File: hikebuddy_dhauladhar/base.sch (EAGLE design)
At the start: 119 parts, among them J1 MF-CON-MICROUSB-RIGHT, J2 GPS Port, J5 SOLDER_PAD_2, J9 47352-1001, U1 LTC3586EUFE-1#PBF, U2 MAX17260SETD+, U3 MF-DSC-SOT233-MMBT3904, U4 MF-DSC-SOT233-MMBT3904, U5 DRV2605LTDGSRQ1, U7 LSM303CTR, U9 LTC6991CDCB#TRMPBF

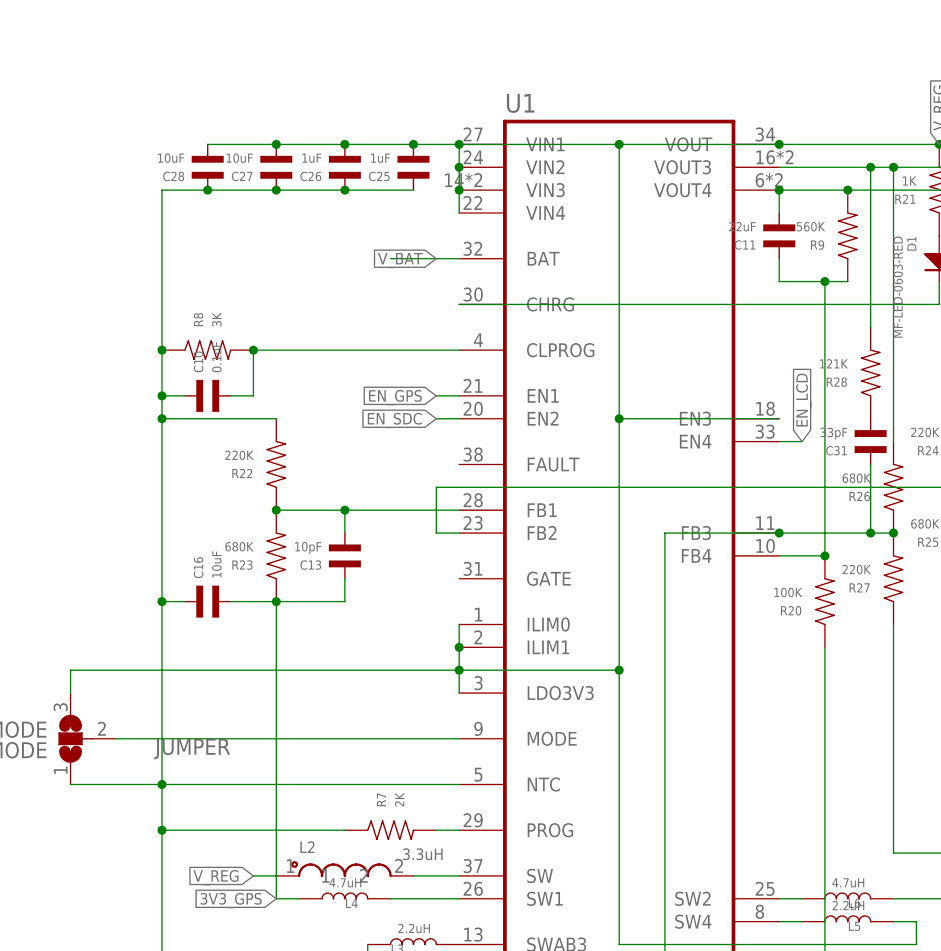
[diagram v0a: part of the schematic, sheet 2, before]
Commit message: pulled up fault and EN to V_REG to fix startup bug
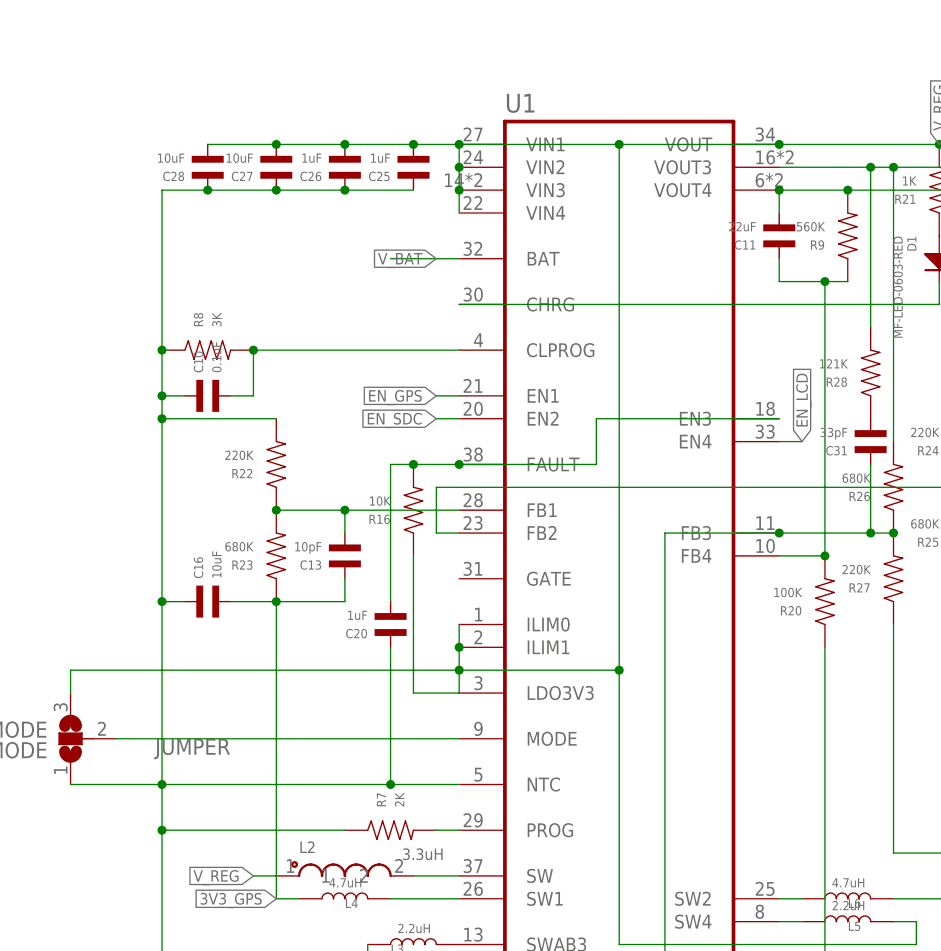
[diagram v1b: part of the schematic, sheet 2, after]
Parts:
- added C20: 1uF, MF_Passives:CAPACITOR_NP_0603
- added R16: 10K, MF_Passives:RESISTOR_0603
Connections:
- new net N$24: C20.P$2, R16.P$2, U1.EN3, U1.FAULT
- net GND: now also C20.P$1
- net V_REG: now also R16.P$1; no longer U1.EN3
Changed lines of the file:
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@@
 <part name="J9" library="47352-1001" deviceset="47352-1001" device="" package3d_urn="urn:adsk.eagle:package:16346114/2"/>
 <part name="GND19" library="supply1" library_urn="urn:adsk.eagle:library:371" deviceset="GND" device=""/>
+<part name="R16" library="MF_Passives" deviceset="RESISTOR" device="_0603" package3d_urn="urn:adsk.eagle:package:16347927/2" value="10K"/>
+<part name="C20" library="MF_Passives" deviceset="CAPACITOR_NP" device="_0603" package3d_urn="urn:adsk.eagle:package:16347923/3" value="1uF"/>
 </parts>
 <sheets>
@@
 <attribute name="VALUE" x="152.4" y="9.906" size="1.778" layer="96" align="top-center"/>
 </instance>
+<instance part="R16" gate="G$1" x="53.34" y="78.74" smashed="yes" rot="R180">
+<attribute name="NAME" x="50.8" y="77.216" size="1.016" layer="95" font="vector" rot="R180" align="top-left"/>
+<attribute name="VALUE" x="50.8" y="80.264" size="1.016" layer="96" font="vector" rot="R180"/>
+</instance>
+<instance part="C20" gate="G$1" x="50.8" y="66.04" smashed="yes" rot="R180">
+<attribute name="NAME" x="48.26" y="64.516" size="1.016" layer="95" font="vector" rot="R180" align="top-left"/>
+<attribute name="VALUE" x="48.26" y="67.564" size="1.016" layer="96" font="vector" rot="R180"/>
+</instance>
 </instances>
 <busses>
@@
 <junction x="25.4" y="91.44"/>
 <pinref part="U1" gate="G$1" pin="NTC"/>
-<wire x1="58.42" y1="48.26" x2="25.4" y2="48.26" width="0.1524" layer="91"/>
+<wire x1="58.42" y1="48.26" x2="50.8" y2="48.26" width="0.1524" layer="91"/>
 <junction x="25.4" y="48.26"/>
+<wire x1="50.8" y1="48.26" x2="25.4" y2="48.26" width="0.1524" layer="91"/>
 <wire x1="25.4" y1="43.18" x2="25.4" y2="5.08" width="0.1524" layer="91"/>
 <pinref part="R22" gate="G$1" pin="P$2"/>
@@
 <pinref part="VREG_MODE" gate="G$1" pin="1"/>
 <wire x1="15.24" y1="48.26" x2="25.4" y2="48.26" width="0.1524" layer="91"/>
+<pinref part="C20" gate="G$1" pin="P$1"/>
+<wire x1="50.8" y1="63.5" x2="50.8" y2="48.26" width="0.1524" layer="91"/>
+<junction x="50.8" y="48.26"/>
 </segment>
 <segment>
@@
 <net name="V_REG" class="0">
 <segment>
+<pinref part="L2" gate="G$1" pin="1"/>
+<wire x1="38.1" y1="38.1" x2="35.56" y2="38.1" width="0.1524" layer="91"/>
+<label x="35.56" y="38.1" size="1.27" layer="95" rot="R180" xref="yes"/>
+</segment>
+<segment>
+<pinref part="R16" gate="G$1" pin="P$1"/>
+<pinref part="U1" gate="G$1" pin="LDO3V3"/>
+<wire x1="53.34" y1="73.66" x2="53.34" y2="58.42" width="0.1524" layer="91"/>
+<wire x1="53.34" y1="58.42" x2="58.42" y2="58.42" width="0.1524" layer="91"/>
 <pinref part="U1" gate="G$1" pin="ILIM1"/>
 <pinref part="U1" gate="G$1" pin="ILIM0"/>
 <wire x1="58.42" y1="63.5" x2="58.42" y2="66.04" width="0.1524" layer="91"/>
-<pinref part="U1" gate="G$1" pin="LDO3V3"/>
 <pinref part="U1" gate="G$1" pin="VOUT"/>
-<wire x1="76.2" y1="60.96" x2="76.2" y2="88.9" width="0.1524" layer="91"/>
-<wire x1="76.2" y1="88.9" x2="76.2" y2="119.38" width="0.1524" layer="91"/>
+<wire x1="76.2" y1="60.96" x2="76.2" y2="119.38" width="0.1524" layer="91"/>
 <wire x1="76.2" y1="119.38" x2="93.98" y2="119.38" width="0.1524" layer="91"/>
 <wire x1="58.42" y1="63.5" x2="58.42" y2="60.96" width="0.1524" layer="91"/>
 <junction x="58.42" y="63.5"/>
-<pinref part="U1" gate="G$1" pin="EN3"/>
-<wire x1="58.42" y1="60.96" x2="58.42" y2="58.42" width="0.1524" layer="91"/>
-<wire x1="93.98" y1="88.9" x2="76.2" y2="88.9" width="0.1524" layer="91"/>
-<junction x="76.2" y="88.9"/>
 <pinref part="C12" gate="G$1" pin="P$2"/>
 <wire x1="93.98" y1="119.38" x2="111.76" y2="119.38" width="0.1524" layer="91"/>
@@
 <wire x1="15.24" y1="60.96" x2="58.42" y2="60.96" width="0.1524" layer="91"/>
 <label x="111.76" y="119.38" size="1.27" layer="95" rot="R90" xref="yes"/>
-</segment>
-<segment>
-<pinref part="L2" gate="G$1" pin="1"/>
-<wire x1="38.1" y1="38.1" x2="35.56" y2="38.1" width="0.1524" layer="91"/>
-<label x="35.56" y="38.1" size="1.27" layer="95" rot="R180" xref="yes"/>
+<wire x1="58.42" y1="58.42" x2="58.42" y2="60.96" width="0.1524" layer="91"/>
 </segment>
 </net>
@@
 </segment>
 </net>
+<net name="N$24" class="0">
+<segment>
+<pinref part="U1" gate="G$1" pin="EN3"/>
+<wire x1="93.98" y1="88.9" x2="73.66" y2="88.9" width="0.1524" layer="91"/>
+<wire x1="73.66" y1="88.9" x2="73.66" y2="83.82" width="0.1524" layer="91"/>
+<pinref part="U1" gate="G$1" pin="FAULT"/>
+<wire x1="73.66" y1="83.82" x2="58.42" y2="83.82" width="0.1524" layer="91"/>
+<pinref part="R16" gate="G$1" pin="P$2"/>
+<wire x1="58.42" y1="83.82" x2="53.34" y2="83.82" width="0.1524" layer="91"/>
+<junction x="58.42" y="83.82"/>
+<pinref part="C20" gate="G$1" pin="P$2"/>
+<wire x1="50.8" y1="68.58" x2="50.8" y2="83.82" width="0.1524" layer="91"/>
+<wire x1="53.34" y1="83.82" x2="50.8" y2="83.82" width="0.1524" layer="91"/>
+<junction x="53.34" y="83.82"/>
+</segment>
+</net>

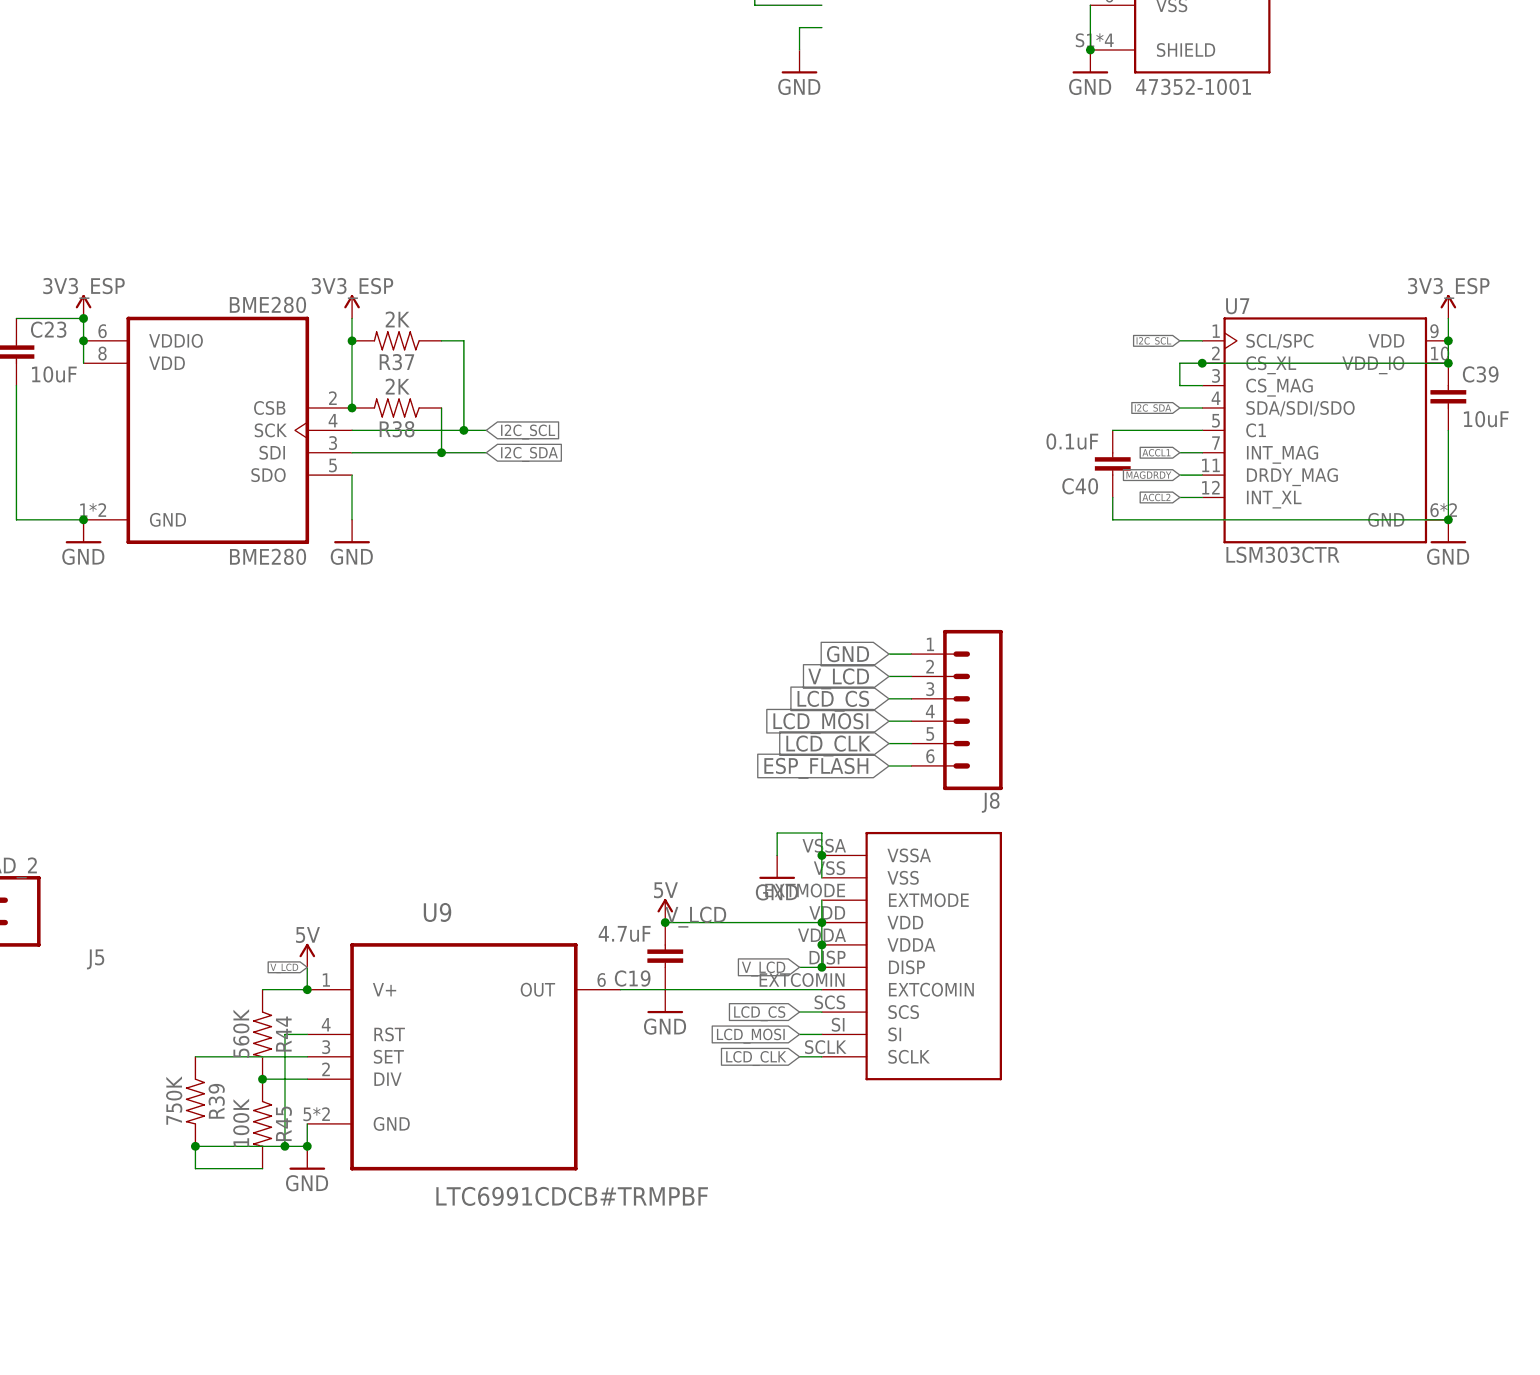
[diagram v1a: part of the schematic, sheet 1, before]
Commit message: replace lsm303 with bmx160
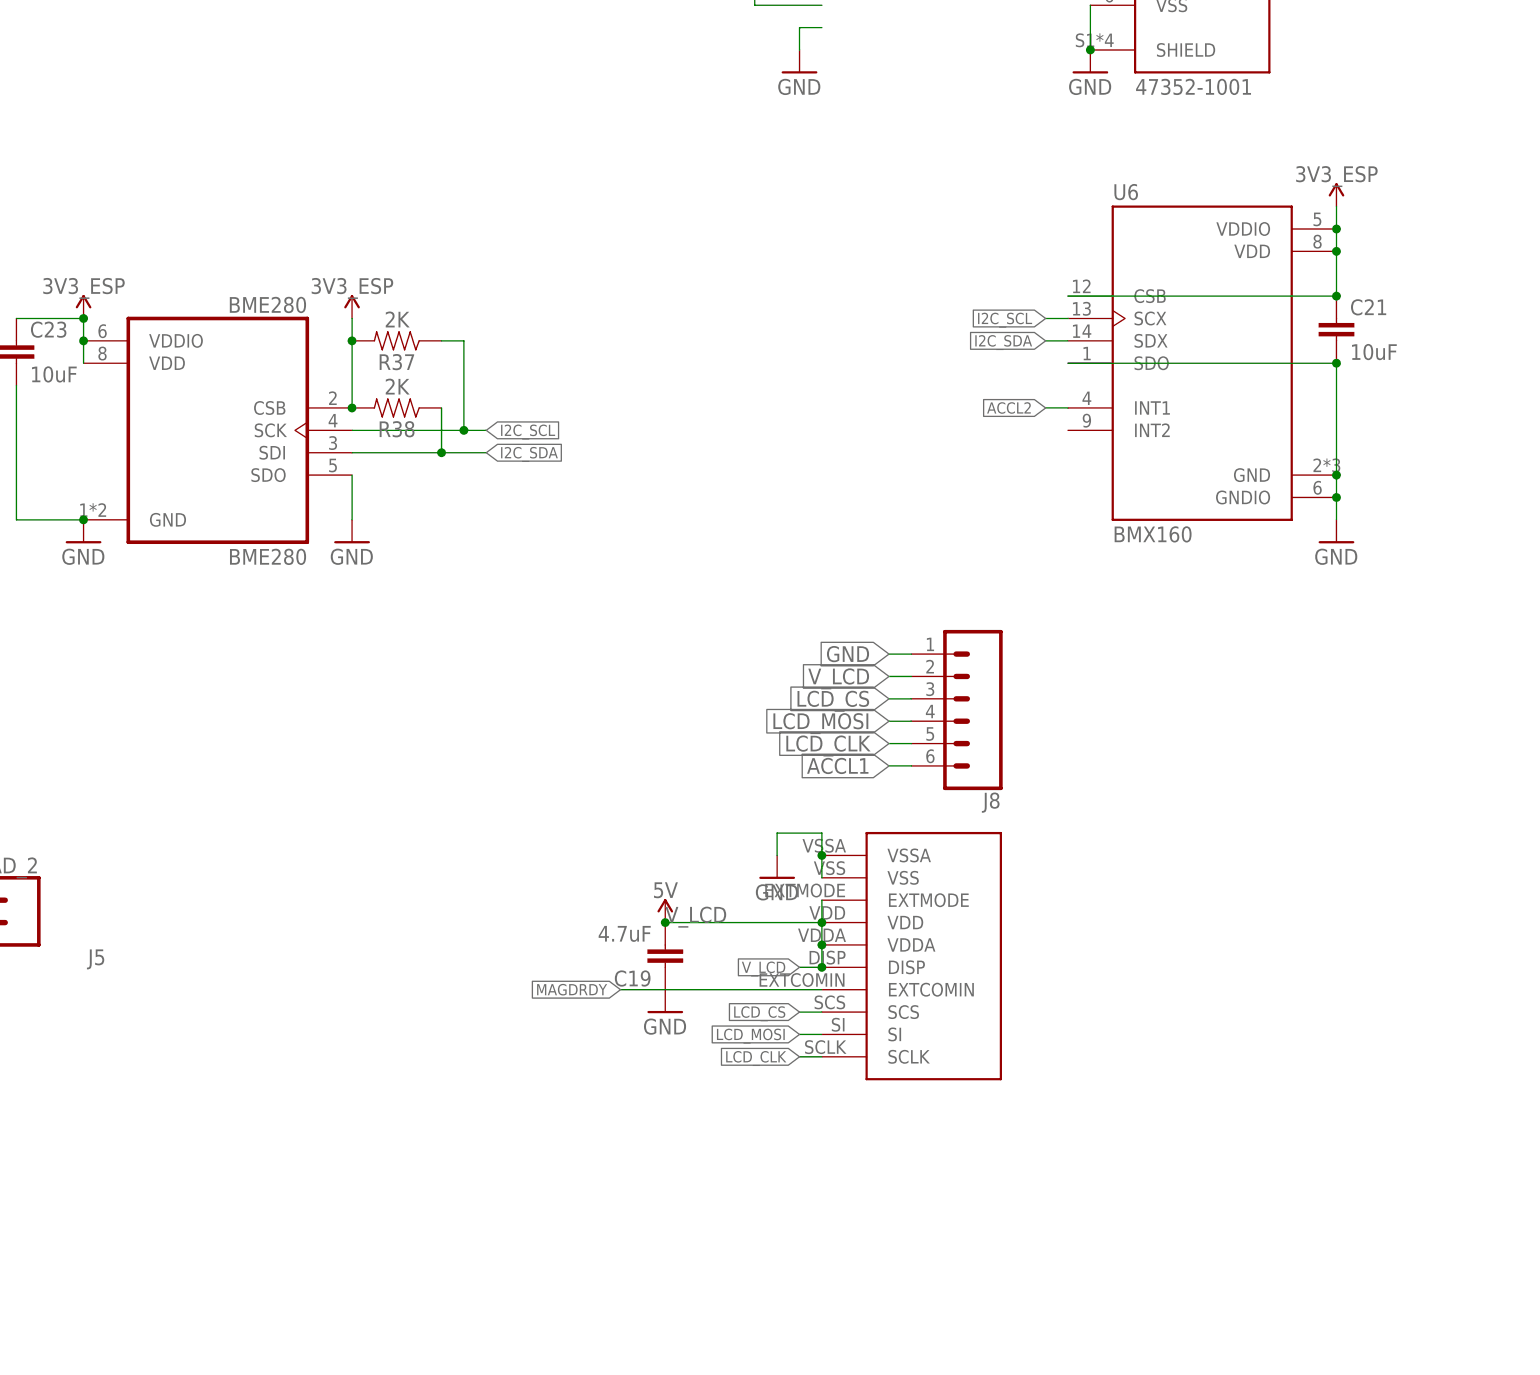
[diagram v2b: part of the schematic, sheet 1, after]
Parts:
- removed C39: 10uF, SparkFun-Capacitors:10UF-0603-6.3V-20%
- removed C40: 0.1uF, SparkFun-Capacitors:4.7UF-0603-6.3V-(10%)
- removed R39: 750K, SparkFun-Resistors:1KOHM-0603-1/10W-1%
- removed R44: 560K, SparkFun-Resistors:1KOHM-0603-1/10W-1%
- removed R45: 100K, SparkFun-Resistors:1KOHM-0603-1/10W-1%
- removed U7: LSM303CTR, LSM303CTR:LSM303CTR
- removed U9: LTC6991CDCB#TRMPBF, LTC6991CS6TRMPBF:LTC6991CS6TRMPBFDFN
- added C21: 10uF, SparkFun-Capacitors:10UF-0603-6.3V-20%
- added U6: BMX160, BMX160:BMX160
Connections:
- removed net N$23: C40.2, U7.C1
- removed net N$35: U$5.EXTCOMIN, U9.OUT
- removed net N$40: R39.1, U9.SET
- removed net N$42: R44.2, R45.1, U9.DIV
- net ACCL1: now also J8.6; no longer U7.INT_MAG
- net ACCL2: now also U6.INT1; no longer U7.INT_XL
- net ESP_FLASH: no longer J8.6
- net GND: now also C21.2, U6.GND, U6.GNDIO, U6.SDO; no longer C39.2, C40.1, R39.2, R45.2, U7.GND, U9.GND, U9.RST
- net I2C_SCL: now also U6.SCX; no longer U7.SCL/SPC
- net I2C_SDA: now also U6.SDX; no longer U7.SDA/SDI/SDO
- net MAGDRDY: now also U$5.EXTCOMIN; no longer U7.DRDY_MAG
- net VCC: now also C21.1, U6.CSB, U6.VDD, U6.VDDIO; no longer C39.1, U7.CS_MAG, U7.CS_XL, U7.VDD, U7.VDD_IO
- net V_LCD: no longer R44.1, U9.V+
